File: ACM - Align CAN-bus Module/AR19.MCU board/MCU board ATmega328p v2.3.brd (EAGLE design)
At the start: 64.1 x 37.8 mm, 42 parts, among them IC1 ATMEGA328P-MMH, IC2 MIC5239-5.0YS_TR, IC3 MCP25625-E_ML, J1 AVR_SPI_PROG_3X2NS

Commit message: Finished .SCH v2.3
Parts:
- removed LED1: SML-A12DTT86, SML-A12DTT86:LEDC1606X125N
- removed P_CANH, P_CANL, P_GND, P_I/O1, P_I/O10, P_I/O11, P_I/O12, P_I/O2, P_I/O3, P_I/O4, P_I/O5, P_I/O6, P_I/O7, P_I/O8, P_I/O9: (no value), wirepad:2,15/1,0
- removed R3: 500Ohm, CRCW040295R3FKED(0402):RESC1005X40N
- added C13: 0.1uF, eagle-ltspice:C0603
- added I/O_AD0, I/O_AD1, I/O_AD2, I/O_AD3, I/O_AD4_SDA, I/O_AD5_SCL, I/O_D0_RX, I/O_D1_TX, I/O_D2_INT: (no value), wirepad:2,15/1,0
- renumbered P_VCC to 12V
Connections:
- net VCC renamed N$3
- removed net DOTS.SDI: DOTSTAR.1, IC1.26
- removed net I/O1: IC1.19, P_I/O1.1
- removed net I/O10: IC1.11, P_I/O10.1
- removed net I/O11: IC1.1, P_I/O11.1
- removed net I/O12: IC1.2, P_I/O12.1
- removed net I/O2: IC1.20, P_I/O2.1
- removed net I/O3: IC1.21, P_I/O3.1
- removed net I/O4: IC1.22, P_I/O4.1
- removed net I/O5: IC1.23, P_I/O5.1
- removed net I/O6: IC1.24, P_I/O9.1
- removed net I/O7: IC1.7, P_I/O8.1
- removed net I/O8: IC1.8, P_I/O7.1
- removed net I/O9: IC1.9, P_I/O6.1
- removed net N$3 (its old number): LED1.1, R3.1
- removed net N$4: IC1.29
- removed net N$8: IC1.27
- removed net SS: IC1.12
- new net CS_DOTS: DOTSTAR.1
- new net DOTS_CS: IC1.10
- new net I/O_AD0: I/O_AD0.1, IC1.19
- new net I/O_AD1: I/O_AD1.1, IC1.20
- new net I/O_AD2: I/O_AD2.1, IC1.21
- new net I/O_AD3: I/O_AD3.1, IC1.22
- new net I/O_AD4_SCL: I/O_AD4_SDA.1, IC1.23
- new net I/O_AD5_SCL: I/O_AD5_SCL.1, IC1.24
- new net I/O_D0_RX: I/O_D0_RX.1, IC1.26
- new net I/O_D1_TX: I/O_D1_TX.1, IC1.27
- new net I/O_D2_INT: I/O_D2_INT.1, IC1.1
- net 5V: now also C13.1, IC1.17
- net CANH: no longer P_CANH.1
- net CANL: no longer P_CANL.1
- net CAN_CS: now also IC1.11; no longer IC1.10
- net GND: now also C13.2, IC1.29, IC2.4; no longer LED1.2, P_GND.1
- net N$2: no longer R3.2

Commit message: Begynt å lage board
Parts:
- moved I/O_AD4_SDA 163.0 mm to (3.17, 73.0)
- moved I/O_AD3 158.9 mm to (6.99, 73.0)
- moved I/O_AD2 154.9 mm to (10.8, 73.0)
- moved I/O_AD1 151.1 mm to (14.6, 73.0)
- moved I/O_AD0 147.5 mm to (19.1, 73.0)
- moved I/O_D1_TX 119.7 mm to (0.00, 16.5)
- moved I/O_AD5_SCL 119.7 mm to (0.00, 25.4)
- moved I/O_D0_RX 119.7 mm to (0.00, 21.0)
- moved I/O_D2_INT 119.7 mm to (0.00, 12.1)
- moved C10 74.1 mm to (-28.6, 19.1)
- moved C13 67.7 mm to (14.6, 28.6), turned to 180 degrees
- moved C12 63.0 mm to (18.4, 28.6)
- moved C11 52.7 mm to (14.6, 17.8), turned to 180 degrees
- moved C7 42.2 mm to (36.8, 20.3)
- moved C8 39.8 mm to (36.2, 15.2)
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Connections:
- removed net CS_DOTS: DOTSTAR.1
- net CAN_MISO: now also IC1.14
- net CAN_MOSI: now also IC1.13
- net DOTS_CS: now also DOTSTAR.1
- net MISO: no longer IC1.14
- net MOSI: no longer IC1.13
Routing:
- net MCU_OSC2: track 0.00 -> 16.3 mm
- net N$2: track 0.00 -> 13.5 mm
- net 5V: track 0.00 -> 11.5 mm
- net SCK: track 0.00 -> 10.9 mm, vias 0 -> 1
- net MCU_OSC1: track 0.00 -> 8.10 mm
- net CAN_MOSI: track 0.00 -> 7.69 mm
- net RESET_MCU: track 0.00 -> 5.61 mm
- net CAN_MISO: track 0.00 -> 3.97 mm, vias 0 -> 2
- net N$3: track 0.00 -> 3.92 mm
- net I/O_D1_TX: track 0.00 -> 2.84 mm, vias 0 -> 1
- net I/O_AD3: track 0.00 -> 2.49 mm, vias 0 -> 1
- net I/O_D0_RX: track 0.00 -> 2.23 mm, vias 0 -> 1
- net I/O_D2_INT: track 0.00 -> 2.15 mm, vias 0 -> 1
- net CAN_INIT: track 0.00 -> 2.11 mm, vias 0 -> 1
- net I/O_AD2: track 0.00 -> 2.07 mm, vias 0 -> 1
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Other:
- board size 64.1 x 37.8 mm -> 64.1 x 38.4 mm

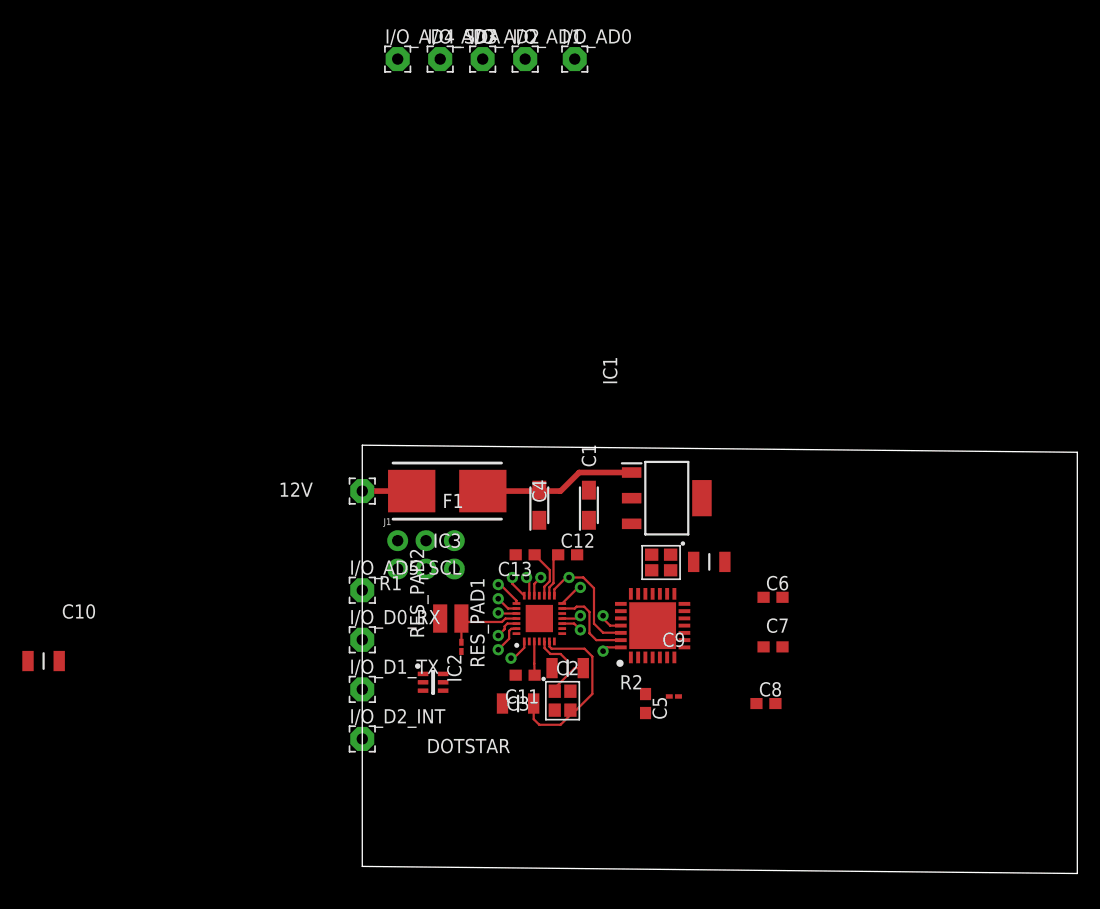
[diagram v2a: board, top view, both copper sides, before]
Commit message: Progress with tracing (40 Air-errors left), Change text size to 20
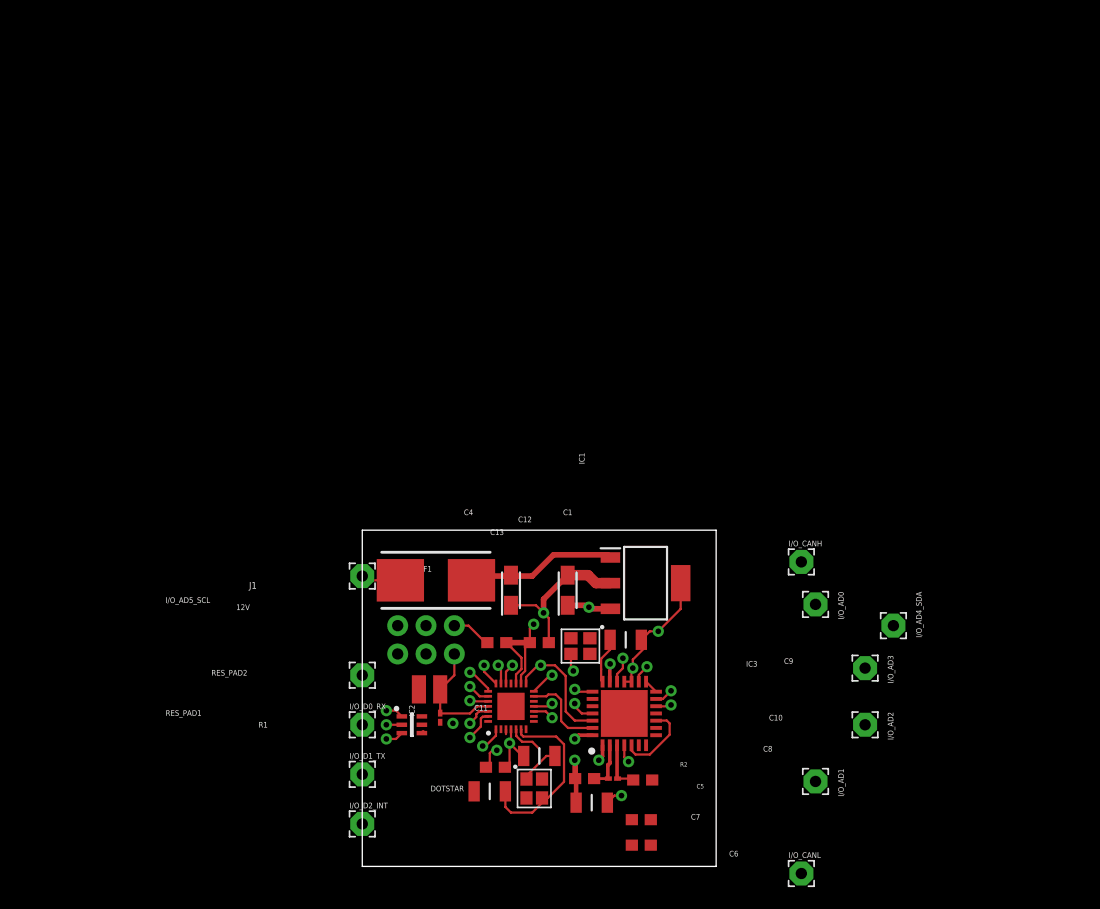
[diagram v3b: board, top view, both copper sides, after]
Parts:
- added I/O_CANH, I/O_CANL: (no value), wirepad:2,15/1,0
- moved I/O_AD1 69.8 mm to (40.6, 8.26), turned to 270 degrees
- moved I/O_AD2 68.8 mm to (45.1, 13.3), turned to 270 degrees
- moved I/O_AD4_SDA 67.5 mm to (47.6, 22.2), turned to 270 degrees
- moved I/O_AD3 66.6 mm to (45.1, 18.4), turned to 270 degrees
- moved I/O_AD0 53.4 mm to (40.6, 24.1), turned to 270 degrees
- moved C10 50.8 mm to (20.6, 6.35)
- moved C6 25.2 mm to (25.0, 2.54)
- moved C7 19.5 mm to (25.0, 4.83)
- moved C8 13.0 mm to (25.1, 8.38)
- moved U$1 10.4 mm to (21.2, 21.8)
- moved C9 10.2 mm to (23.6, 21.0)
- moved R2 9.17 mm to (22.5, 8.51)
- moved C11 8.68 mm to (11.9, 9.53), turned to 0 degrees
- moved C5 8.67 mm to (19.9, 8.51), turned to 180 degrees
- moved C3 8.27 mm to (11.4, 7.37)
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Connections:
- net N$1 renamed MCP_RESET
- net N$2 renamed 12V_FUSED
- net N$3 renamed 12V_UNFUSED
- net CANH: now also I/O_CANH.1
- net CANL: now also I/O_CANL.1
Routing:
- net GND: track 0.00 -> 43.9 mm, vias 0 -> 7
- net 5V: track 11.5 -> 50.3 mm, vias 0 -> 5
- net SCK: track 10.9 -> 32.4 mm, vias 1 -> 2
- net DOTS_CS: track 1.87 -> 23.1 mm, vias 1 -> 2
- net CAN_OSC2: track 0.00 -> 20.6 mm, vias 0 -> 3
- net I/O_D2_INT: track 2.15 -> 15.5 mm
- net TXCAN: track 0.00 -> 12.5 mm, vias 0 -> 2
- net I/O_D0_RX: track 2.23 -> 13.3 mm
- net I/O_D1_TX: track 2.84 -> 13.5 mm
- net CAN_CS: track 1.74 -> 11.2 mm, vias 1 -> 2
- net RXCAN: track 0.00 -> 7.12 mm
- net MCP_RESET: track 0.00 -> 4.41 mm
- net CAN_OSC1: track 0.00 -> 4.15 mm
- net RESET_MCU: track 5.61 -> 9.15 mm
- net MOSI: track 0.00 -> 1.80 mm
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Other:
- board size 64.1 x 38.4 mm -> 31.7 x 30.1 mm

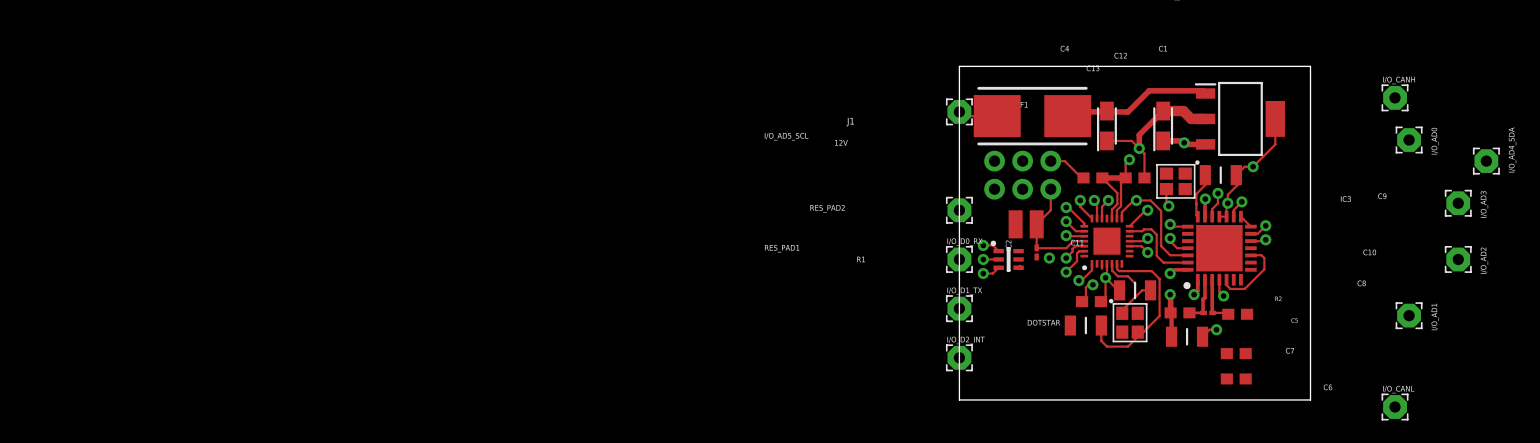
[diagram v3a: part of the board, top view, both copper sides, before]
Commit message: ADDED: Support for Half cut/castellated holes.
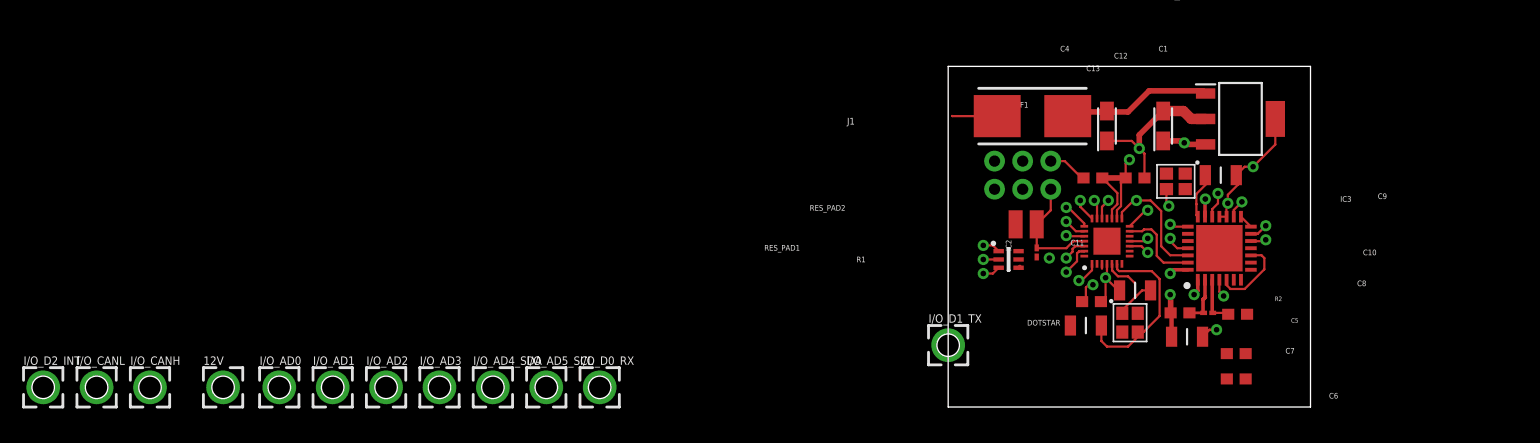
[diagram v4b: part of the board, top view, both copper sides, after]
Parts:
- 12V, I/O_AD0, I/O_AD1, I/O_AD2, I/O_AD3, I/O_AD4_SDA, I/O_AD5_SCL, I/O_CANH, I/O_CANL, I/O_D0_RX, I/O_D1_TX, I/O_D2_INT: device wirepad:2,15/1,0 -> wirepad_edit:2,54/2,0(HALFHOLE)H+V
- moved I/O_CANL 117.4 mm to (-78.0, 1.78)
- moved I/O_CANH 115.5 mm to (-73.2, 1.78)
- moved I/O_AD0 104.5 mm to (-61.5, 1.78), turned to 0 degrees
- moved I/O_AD2 97.6 mm to (-51.8, 1.78), turned to 0 degrees
- moved I/O_AD1 97.5 mm to (-56.6, 1.78), turned to 0 degrees
- moved I/O_AD3 93.6 mm to (-47.0, 1.78), turned to 0 degrees
- moved I/O_AD4_SDA 92.1 mm to (-42.2, 1.78), turned to 0 degrees
- moved I/O_D2_INT 82.8 mm to (-82.8, 1.78)
- moved 12V 71.1 mm to (-66.5, 1.78)
- moved I/O_AD5_SCL 40.6 mm to (-37.3, 1.78)
- moved I/O_D0_RX 34.5 mm to (-32.5, 1.78)
- moved I/O_D1_TX 3.45 mm to (-1.02, 5.59)
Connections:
- net 12V_UNFUSED: now also 12V.P$1; no longer 12V.1
- net CANH: now also I/O_CANH.P$1; no longer I/O_CANH.1
- net CANL: now also I/O_CANL.P$1; no longer I/O_CANL.1
- net I/O_AD0: now also I/O_AD0.P$1; no longer I/O_AD0.1
- net I/O_AD1: now also I/O_AD1.P$1; no longer I/O_AD1.1
- net I/O_AD2: now also I/O_AD2.P$1; no longer I/O_AD2.1
- net I/O_AD3: now also I/O_AD3.P$1; no longer I/O_AD3.1
- net I/O_AD4_SCL: now also I/O_AD4_SDA.P$1; no longer I/O_AD4_SDA.1
- net I/O_AD5_SCL: now also I/O_AD5_SCL.P$1; no longer I/O_AD5_SCL.1
- net I/O_D0_RX: now also I/O_D0_RX.P$1; no longer I/O_D0_RX.1
- net I/O_D1_TX: now also I/O_D1_TX.P$1; no longer I/O_D1_TX.1
- net I/O_D2_INT: now also I/O_D2_INT.P$1; no longer I/O_D2_INT.1
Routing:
- net I/O_D2_INT: track 15.5 -> 8.79 mm
- net I/O_D0_RX: track 13.3 -> 10.2 mm
- net I/O_D1_TX: track 13.5 -> 15.2 mm
- net 12V_UNFUSED: track 3.07 -> 4.09 mm
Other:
- board size 31.7 x 30.1 mm -> 32.7 x 30.8 mm

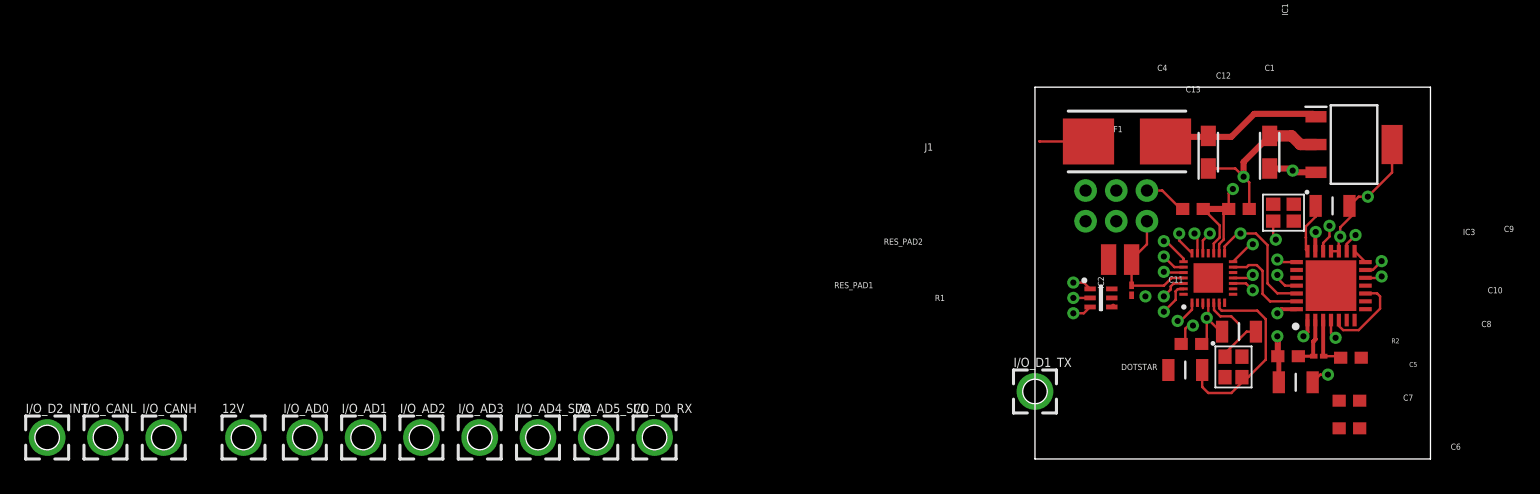
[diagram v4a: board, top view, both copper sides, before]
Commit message: Deleted AD0 and minor changes to board file
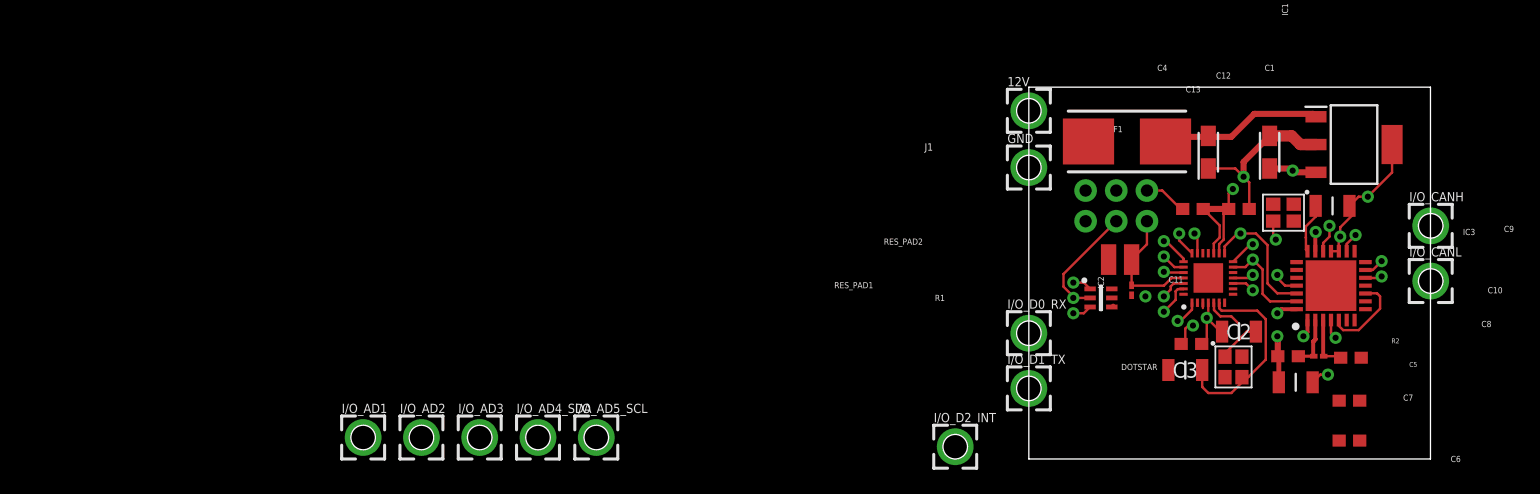
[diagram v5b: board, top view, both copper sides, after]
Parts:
- removed I/O_AD0: (no value), wirepad_edit:2,54/2,0(HALFHOLE)H+V
- added GND: (no value), wirepad_edit:2,54/2,0(HALFHOLE)H+V
- moved I/O_CANL 110.5 mm to (31.8, 14.7)
- moved I/O_CANH 106.4 mm to (31.8, 19.3)
- moved I/O_D2_INT 75.2 mm to (-7.62, 1.02)
- moved 12V 70.4 mm to (-1.52, 28.8)
- moved I/O_D0_RX 32.2 mm to (-1.52, 10.4)
- moved C6 1.02 mm to (25.0, 1.52)
- moved I/O_D1_TX 0.57 mm to (-1.52, 5.84)
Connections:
- removed net CAN_MISO: IC1.14, IC3.28
- removed net CAN_MOSI: IC1.13, IC3.27
- removed net I/O_AD0: I/O_AD0.P$1, IC1.19
- net GND: now also GND.P$1
- net MISO: now also IC1.14, IC3.28
- net MOSI: now also IC1.13, IC3.27
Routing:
- net MOSI: track 1.80 -> 23.9 mm, vias 0 -> 1
- net MISO: track 0.00 -> 19.5 mm, vias 0 -> 2
- net CAN_MOSI: track 7.69 -> 0.00 mm
- net CAN_MISO: track 3.97 -> 0.00 mm, vias 2 -> 0
- net 12V_UNFUSED: track 4.09 -> 0.18 mm
- net GND: track 43.9 -> 40.9 mm, vias 7 -> 6
- net I/O_AD0: track 1.87 -> 0.00 mm, vias 1 -> 0
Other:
- board size 32.7 x 30.8 mm -> 33.3 x 30.8 mm
